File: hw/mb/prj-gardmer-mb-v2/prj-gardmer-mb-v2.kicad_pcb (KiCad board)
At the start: 2 copper layers, 156 parts, among them J1 Conn_01x05, J2 230VAC_IN, J3 Conn_01x04, J4 5VDC_IN, K1 AZ9371T-1A-5D, K2 AZ9371T-1A-5D, K3 AZ9371T-1A-5D, K4 AZ9371T-1A-5D, Q1 BC817, Q13 BC817, Q14 BC817, Q2 BC817, Q3 BC817, Q4 BC817, Q5 BC807, Q6 BC807, Q7 BC807, Q8 BC807, Q9 BC817, SW1 Reset_SW, SW10 Unlock_SW, SW2 Clear_SW, SW3 Minutes_SW, SW4 Hours_SW, SW5 Mode_SW, SW6 Relay1_SW, SW7 Relay2_SW, SW8 Relay3_SW, SW9 Relay4_SW, U1 PIC18F25Q10, U2 PCF8523T, U3 74LS166, U4 74HC595, U5 74HC595, U6 ULN2803A, U7 KW4-804AVB, U8 74HC595, Y1 8MHz, Y2 32.768kHz

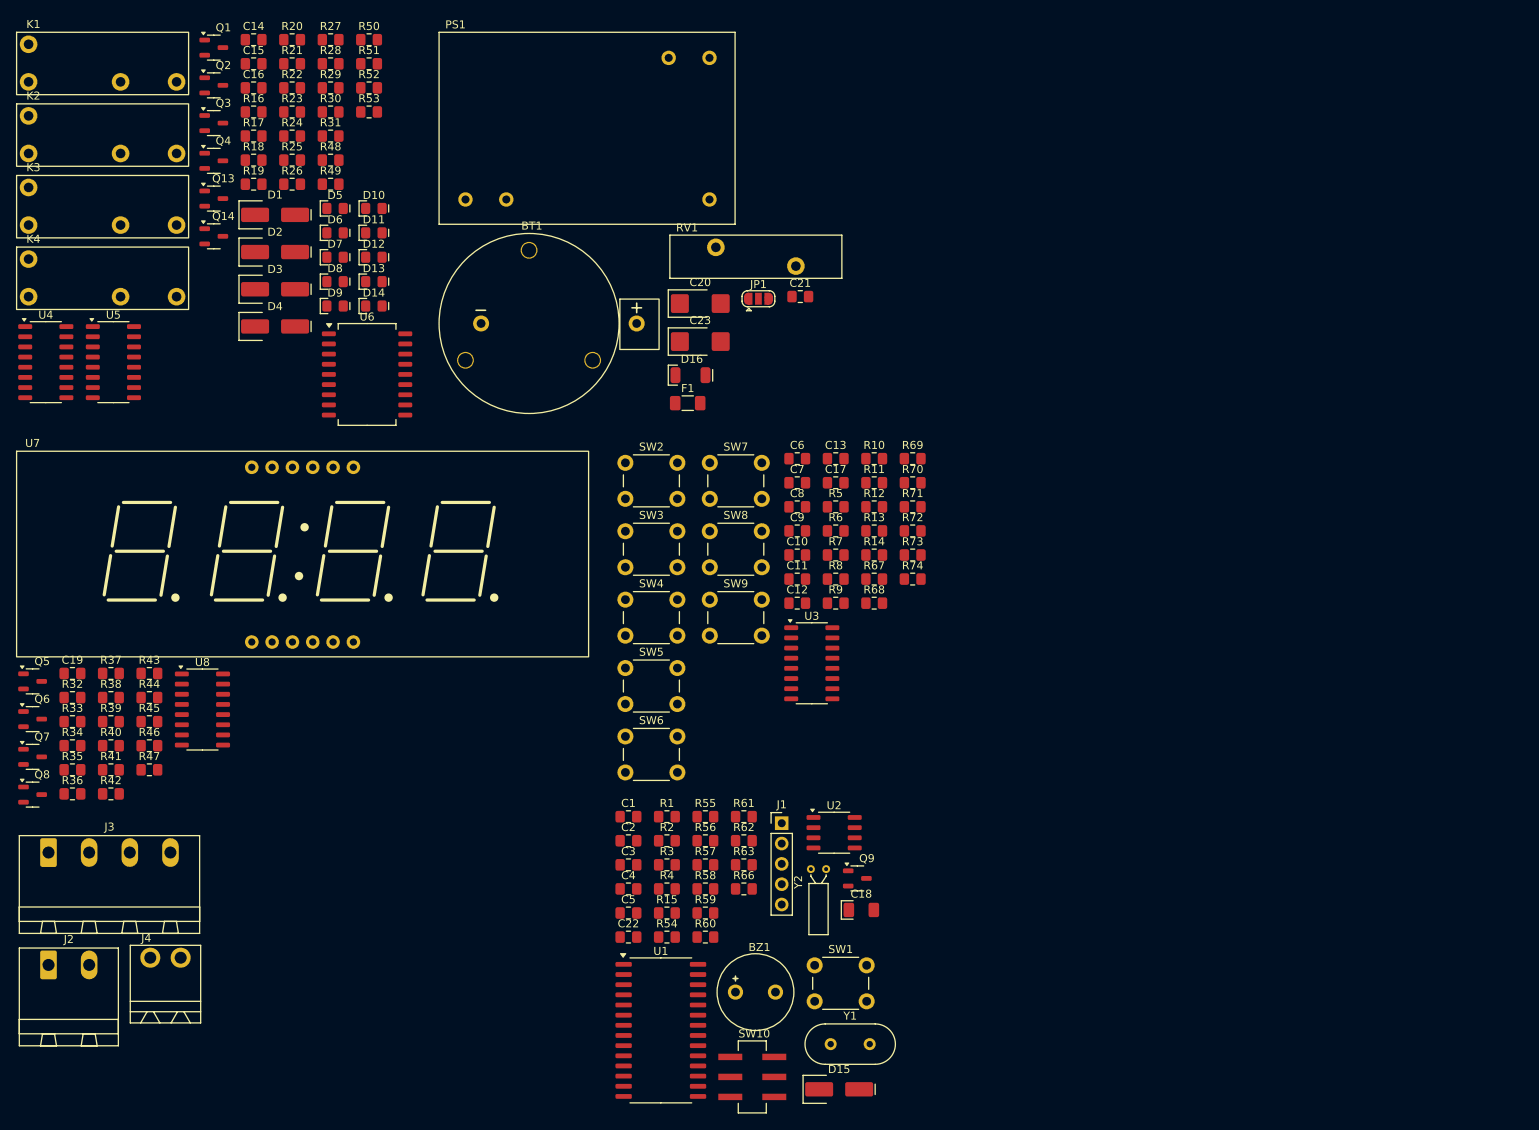
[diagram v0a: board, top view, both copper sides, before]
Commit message: Updated PCB: initially placed elements. Added footprints: holes 4.2mm, 4.4mm and 4.6mm.
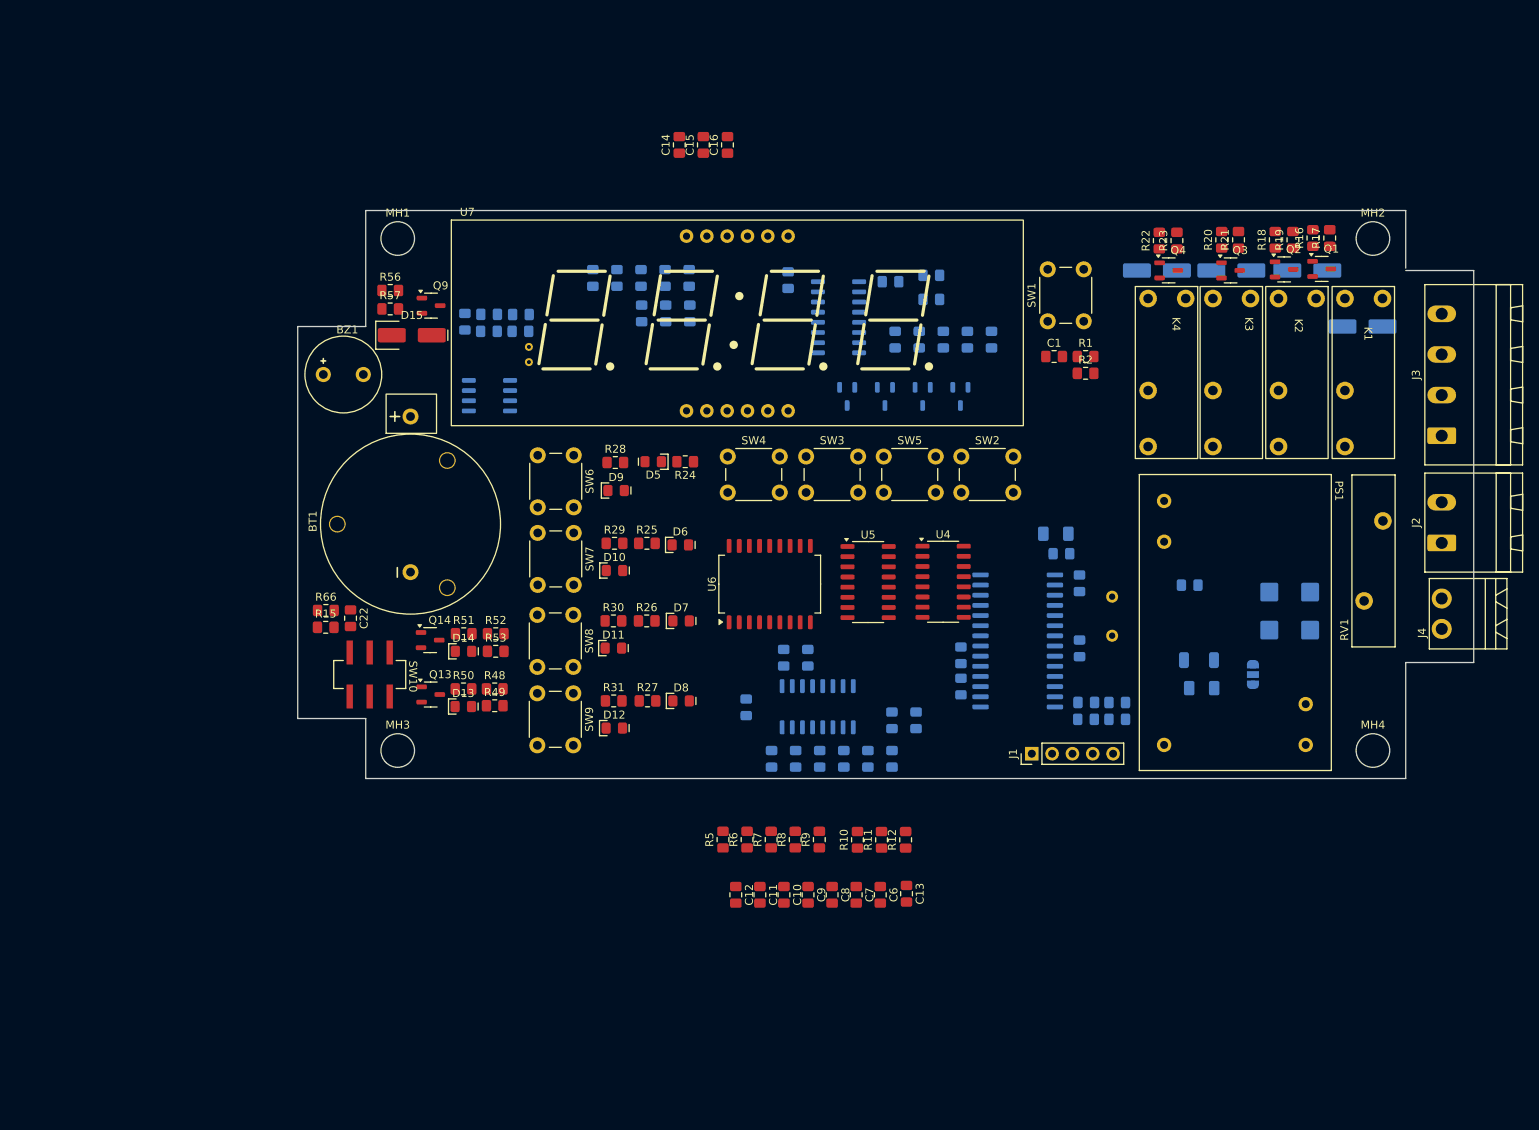
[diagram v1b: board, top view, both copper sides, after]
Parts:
- added MH1: Hole_4.2mm, alf64:Hole_4.2mm, F.Cu at (87.5, 58.8)
- added MH2: Hole_4.2mm, alf64:Hole_4.2mm, F.Cu at (209.4, 58.8)
- added MH3: Hole_4.2mm, alf64:Hole_4.2mm, F.Cu at (87.5, 122.8)
- added MH4: Hole_4.2mm, alf64:Hole_4.2mm, F.Cu at (209.4, 122.8)
- C17, C18, C19, C2, C20, C21, C23, C3, C4, C5, D1, D16, D2, D3, D4, F1, JP1, Q5, Q6, Q7, Q8, R13, R14, R3, R32, R33, R34, R35, R36, R37, R38, R39, R4, R40, R41, R42, R43, R44, R45, R46, R47, R54, R55, R58, R59, R60, R61, R62, R63, R67, R68, R69, R70, R71, R72, R73, R74, U1, U2, U3, U8, Y1, Y2: moved to B.Cu
- moved J2 185.3 mm to (222.0, 94.3), turned to 90 degrees
- moved J3 182.0 mm to (222.0, 75.8), turned to 90 degrees
- moved J4 169.3 mm to (221.3, 105.7), turned to 90 degrees
- moved K1 162.3 mm to (208.2, 75.5), turned to -90 degrees
- moved K2 152.3 mm to (199.9, 75.5), turned to -90 degrees
- moved K3 142.6 mm to (191.7, 75.5), turned to -90 degrees
- moved Q1 141.2 mm to (203.0, 62.6)
- moved D1 136.6 mm to (208.1, 69.8)
- moved Q2 135.8 mm to (198.3, 62.7)
- moved R17 135.1 mm to (204.0, 58.7), turned to 90 degrees
- moved K4 133.6 mm to (183.6, 75.5), turned to -90 degrees
- moved R16 133.3 mm to (201.9, 58.7), turned to 90 degrees
- moved R19 130.1 mm to (199.4, 59.0), turned to 90 degrees
- moved D2 129.1 mm to (201.2, 62.8)
- moved Q3 128.4 mm to (191.6, 62.8)
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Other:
- board outline added: 147 x 71 mm

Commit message: Updated schematic: - added test points instead of connections between relays and outputs - fixed crystal connection for rtc
Updated PCB:
- halfway through the routing

Updated footprints:
- added footprints for test points
- reduced size of pads for D_SMA
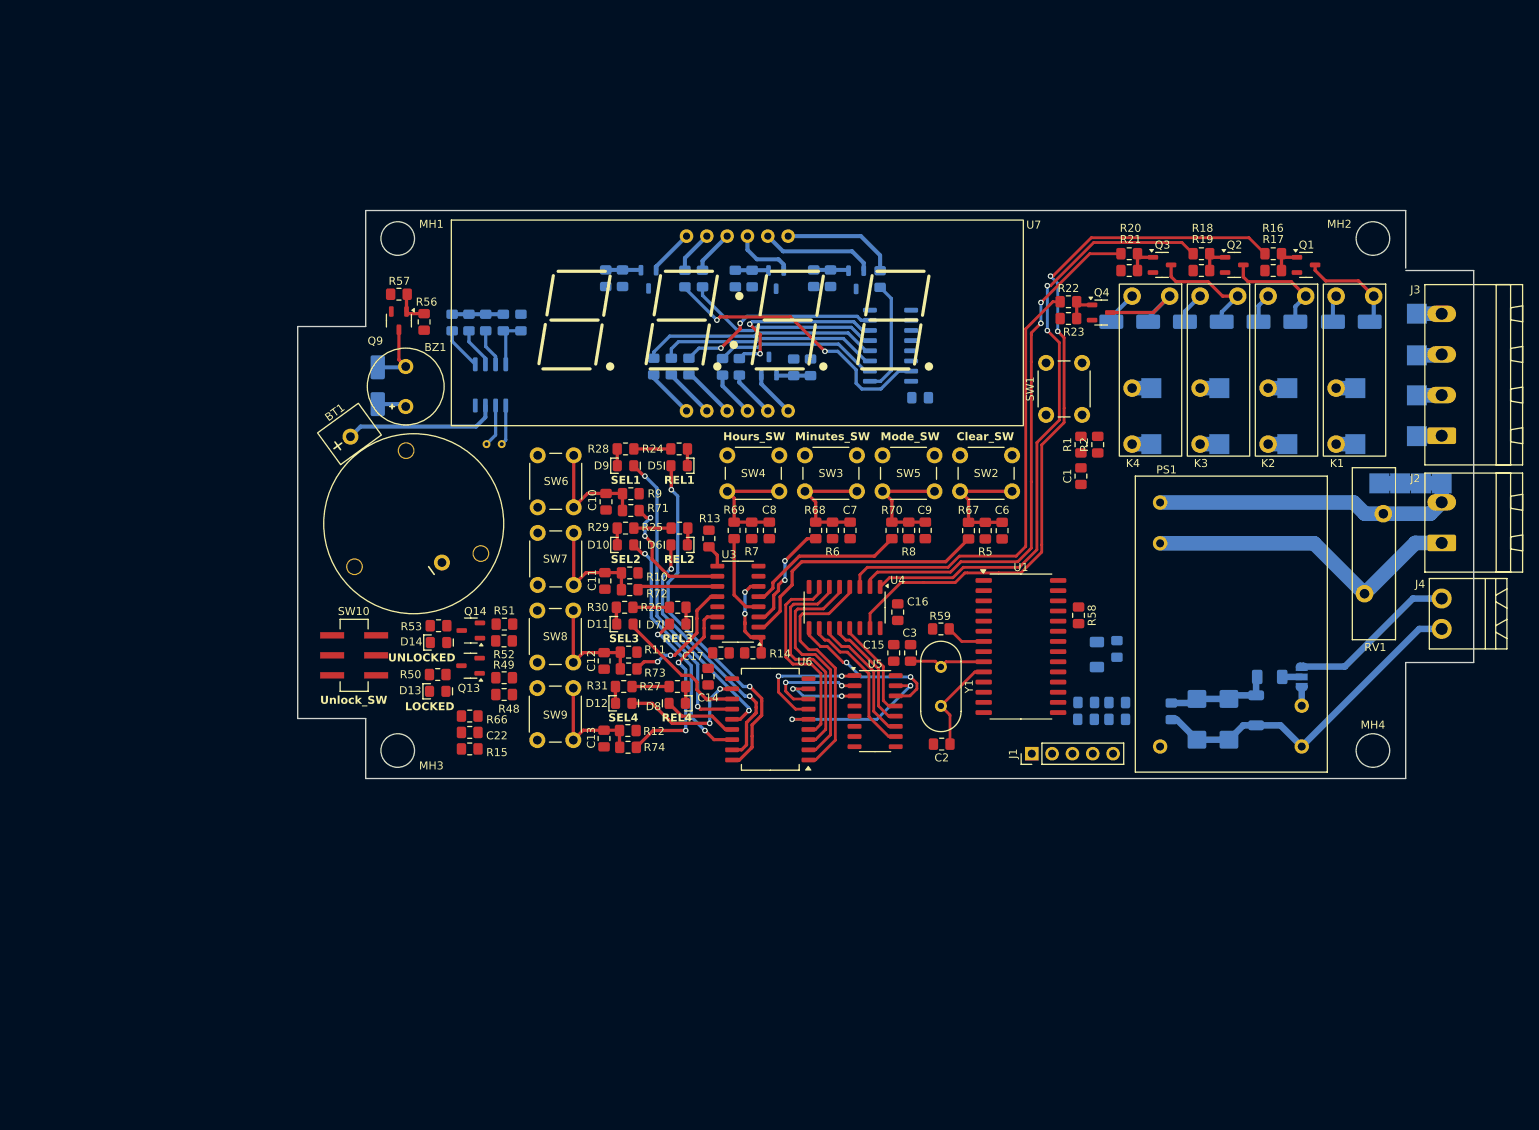
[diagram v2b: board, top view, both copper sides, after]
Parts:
- added TP1: L-1, alf64:TestPoint_Pad_2.5x2.5mm_NoBorders, B.Cu at (218.0, 89.4)
- added TP11: O-1, alf64:TestPoint_Pad_2.5x2.5mm_NoBorders, B.Cu at (207.2, 77.5)
- added TP12: O-2, alf64:TestPoint_Pad_2.5x2.5mm_NoBorders, B.Cu at (198.7, 77.5)
- added TP13: O-3, alf64:TestPoint_Pad_2.5x2.5mm_NoBorders, B.Cu at (190.2, 77.5)
- added TP14: O-4, alf64:TestPoint_Pad_2.5x2.5mm_NoBorders, B.Cu at (181.7, 77.5)
- added TP15: 0-4, alf64:TestPoint_Pad_2.5x2.5mm_NoBorders, B.Cu at (214.9, 68.2)
- added TP16: 0-3, alf64:TestPoint_Pad_2.5x2.5mm_NoBorders, B.Cu at (214.9, 73.4)
- added TP17: 0-2, alf64:TestPoint_Pad_2.5x2.5mm_NoBorders, B.Cu at (214.9, 78.4)
- added TP18: 0-1, alf64:TestPoint_Pad_2.5x2.5mm_NoBorders, B.Cu at (214.9, 83.5)
- added TP2: L-2, alf64:TestPoint_Pad_2.5x2.5mm_NoBorders, B.Cu at (215.4, 89.4)
- added TP3: L-3, alf64:TestPoint_Pad_2.5x2.5mm_NoBorders, B.Cu at (212.8, 89.4)
- added TP4: L-4, alf64:TestPoint_Pad_2.5x2.5mm_NoBorders, B.Cu at (210.2, 89.4)
- added TP5: L-1, alf64:TestPoint_Pad_2.5x2.5mm_NoBorders, B.Cu at (207.2, 84.5)
- added TP6: L-2, alf64:TestPoint_Pad_2.5x2.5mm_NoBorders, B.Cu at (198.7, 84.5)
- added TP7: L-3, alf64:TestPoint_Pad_2.5x2.5mm_NoBorders, B.Cu at (190.2, 84.5)
- added TP8: L-4, alf64:TestPoint_Pad_2.5x2.5mm_NoBorders, B.Cu at (181.7, 84.5)
- C17, C2, C3, R13, R14, R58, R59, R67, R68, R69, R70, R71, R72, R73, R74, U1, U3, Y1: moved to F.Cu
- D15: moved to B.Cu
- moved C15 67.8 mm to (149.5, 110.6)
- moved C14 66.6 mm to (126.3, 113.6), turned to -90 degrees
- moved C16 62.2 mm to (150.0, 105.5)
- moved C10 53.9 mm to (113.5, 91.7)
- moved R5 50.7 mm to (160.9, 95.3)
- moved R9 49.2 mm to (116.6, 90.7), turned to 180 degrees
- moved C6 48.0 mm to (163.1, 95.3)
- moved C9 47.9 mm to (153.4, 95.3)
- moved C8 46.2 mm to (133.9, 95.3)
- moved C7 45.6 mm to (144.1, 95.3)
- moved R10 43.9 mm to (116.5, 100.6), turned to 180 degrees
- moved C11 43.8 mm to (113.4, 101.6)
- moved C13 42.5 mm to (113.3, 121.3)
- moved R8 41.2 mm to (151.4, 95.3)
- moved R6 40.1 mm to (141.8, 95.3)
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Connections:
- J2 pad 1: /230VAC_L -> /230VAC_N
- J2 pad 2: /230VAC_N -> /230VAC_L
- J4 pad 1: /Power/5VDC_IN -> GND
- J4 pad 2: GND -> /Power/5VDC_IN
- K1 pad 1: +5V -> Net-(D1-A)
- K1 pad 2: Net-(D1-A) -> +5V
- K1 pad 3: /230VAC_L -> Net-(K1-Pad3)
- K1 pad 4: /RelaysLeds/RELAY1_OUT -> Net-(K1-Pad4)
- K2 pad 1: +5V -> Net-(D2-A)
- K2 pad 2: Net-(D2-A) -> +5V
- K2 pad 3: /230VAC_L -> Net-(K2-Pad3)
- K2 pad 4: /RelaysLeds/RELAY2_OUT -> Net-(K2-Pad4)
- K3 pad 1: +5V -> Net-(D3-A)
- K3 pad 2: Net-(D3-A) -> +5V
- K3 pad 3: /230VAC_L -> Net-(K3-Pad3)
- K3 pad 4: /RelaysLeds/RELAY3_OUT -> Net-(K3-Pad4)
- K4 pad 1: +5V -> Net-(D4-A)
- K4 pad 2: Net-(D4-A) -> +5V
- K4 pad 3: /230VAC_L -> Net-(K4-Pad3)
- K4 pad 4: /RelaysLeds/RELAY4_OUT -> Net-(K4-Pad4)
- U2 pad 2: Net-(U2-OSCI) -> Net-(U2-OSCO)
- Y2 pad 2: Net-(U2-OSCI) -> Net-(U2-OSCO)
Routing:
- net /RelaysLeds/RELAY1_EN: track 0.00 -> 92.5 mm, vias 0 -> 2
- net /RelaysLeds/RELAY2_EN: track 0.00 -> 77.3 mm, vias 0 -> 2
- net /RelaysLeds/RELAY3_EN: track 0.00 -> 66.4 mm, vias 0 -> 2
- net +5V: track 0.00 -> 57.6 mm
- net /RelaysLeds/RELAY4_EN: track 0.00 -> 56.6 mm
- net /230VAC_L: track 0.00 -> 46.5 mm
- net Net-(D5-K): track 0.00 -> 45.0 mm, vias 0 -> 2
- net GND: track 0.00 -> 42.8 mm
- net /230VAC_N: track 0.00 -> 40.4 mm
- net Net-(D9-K): track 0.00 -> 39.2 mm, vias 0 -> 2
- net Net-(U8-QA): track 0.00 -> 35.9 mm, vias 0 -> 2
- net Net-(D6-K): track 0.00 -> 33.3 mm, vias 0 -> 2
- net Net-(U3-A): track 0.00 -> 32.9 mm
- net /RelaysLeds/RELAY_LED1_EN: track 0.00 -> 30.4 mm
- net Net-(U8-QE): track 0.00 -> 29.7 mm
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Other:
- board text added: "LOCKED"
- board text added: "REL1"
- board text added: "REL2"
- board text added: "REL3"
- board text added: "REL4"
- board text added: "SEL1"
- board text added: "SEL2"
- board text added: "SEL3"
- board text added: "SEL4"
- board text added: "UNLOCKED"
- board text added: "Unlock_SW"

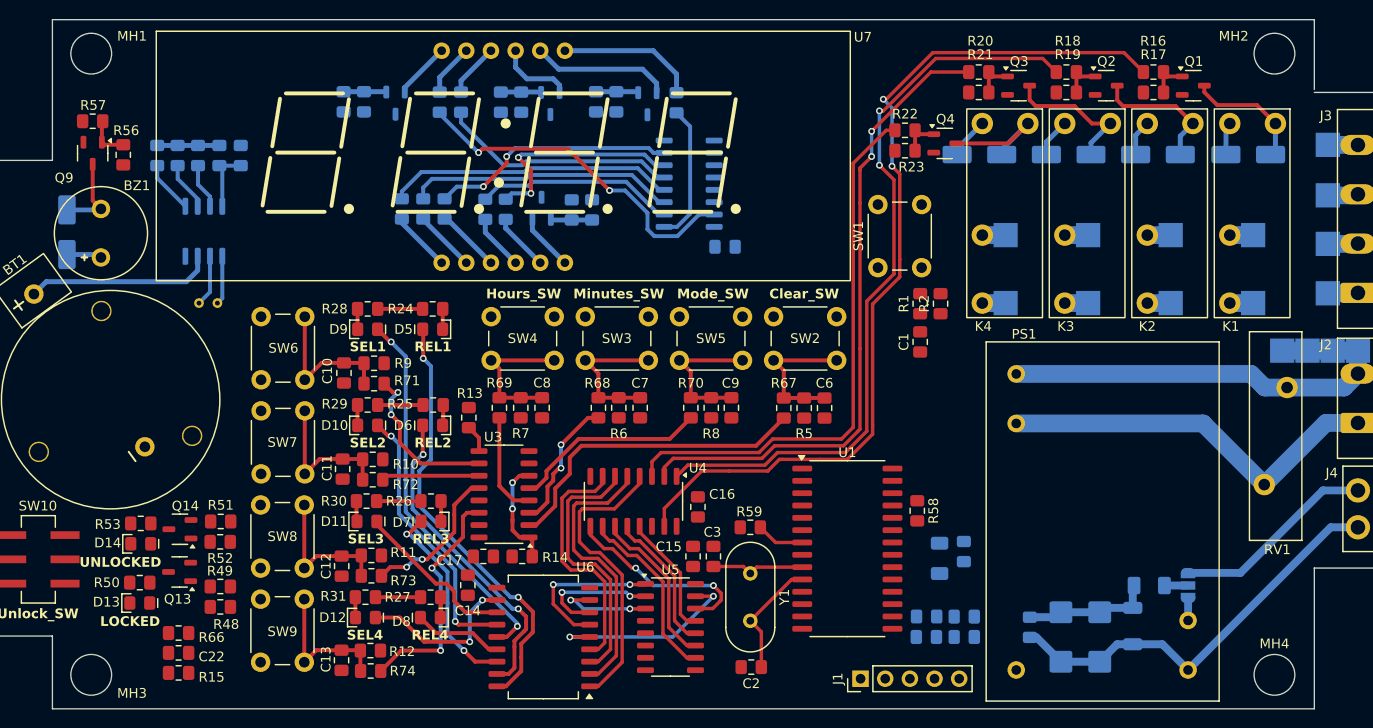
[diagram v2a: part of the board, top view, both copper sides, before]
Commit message: Updated footprints: - changed diodes footprints pad numbers, so the diode 'bar' (cathode) now points to the silkscreen mark
Updated PCB:
- updated all diode footprints
- fixed board outline (it was not closed), so the 3D view now presents correct board shape
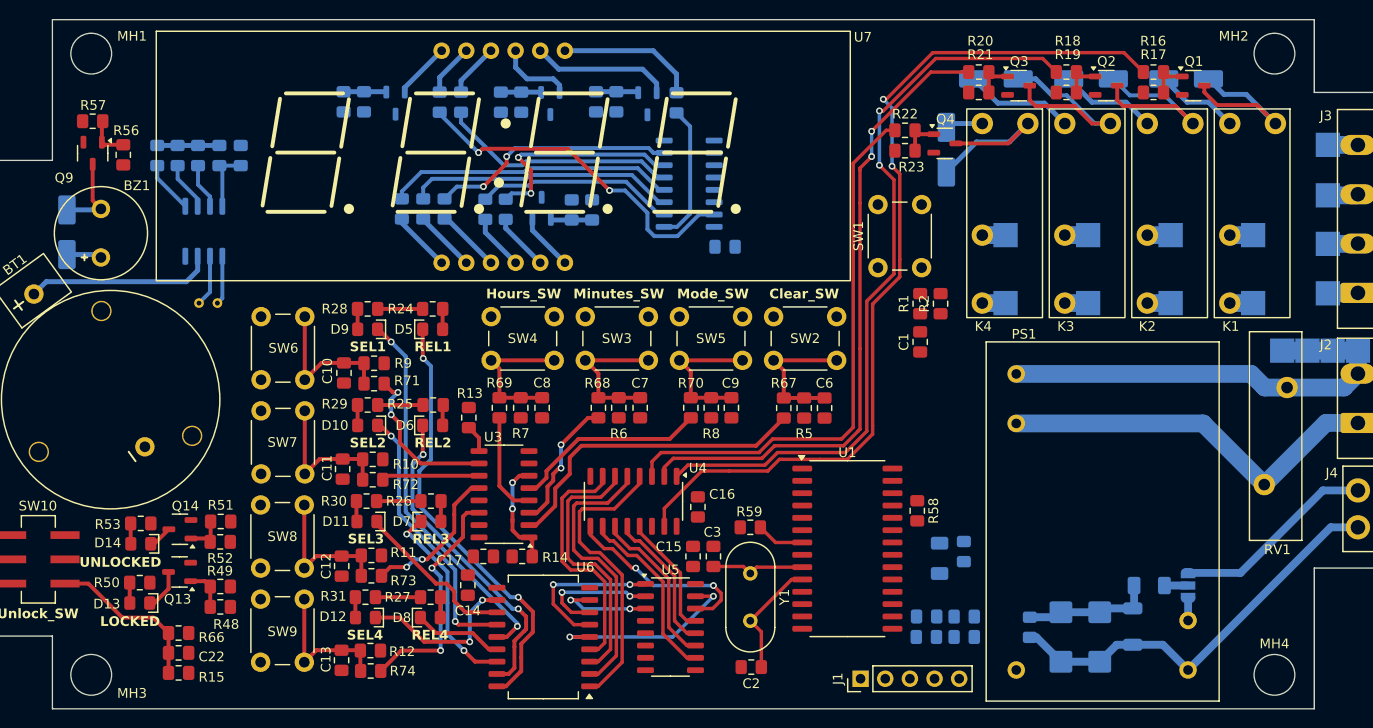
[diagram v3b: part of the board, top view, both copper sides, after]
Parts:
- moved D3 10.8 mm to (180.7, 61.4), turned to 0 degrees
- moved D2 10.4 mm to (190.5, 61.4), turned to 0 degrees
- moved D1 10.1 mm to (200.3, 61.4), turned to 0 degrees
- moved D4 3.44 mm to (175.6, 68.7), turned to -90 degrees
- turned D10 to 180 degrees
- turned D11 to 180 degrees
- turned D12 to 180 degrees
- turned D13 to 180 degrees
- turned D14 to 180 degrees
- turned D15 to 90 degrees
- turned D16 to -90 degrees
- turned D5 to 0 degrees
- turned D6 to 0 degrees
- turned D7 to 0 degrees
- turned D8 to 0 degrees
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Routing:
- net +5V: track 57.6 -> 76.6 mm
- net Net-(C22-Pad1): track 0.00 -> 16.9 mm
- net Net-(D3-A): track 14.8 -> 22.2 mm
- net Net-(D2-A): track 14.0 -> 20.4 mm
- net Net-(D4-A): track 12.6 -> 18.7 mm
- net Net-(D1-A): track 12.7 -> 18.1 mm
- net Net-(Q13-B): track 0.00 -> 4.35 mm
- net Net-(D13-K): track 0.00 -> 4.28 mm
- net Net-(Q14-B): track 0.00 -> 4.24 mm
- net Net-(D14-K): track 0.00 -> 2.50 mm
- net Net-(D13-A): track 0.00 -> 2.11 mm
- net Net-(D14-A): track 0.00 -> 2.11 mm
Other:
- outline, holes or cut-outs redrawn
